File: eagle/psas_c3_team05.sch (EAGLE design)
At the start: 92 parts, among them IC1 CP2102, J1 3220-10-0100-00, J2 1.27MM_HDR_2X12X1, U1 MIC5319 3.3V, U2 MCP73871, U3 MKW01Z128, X1 32 MHz

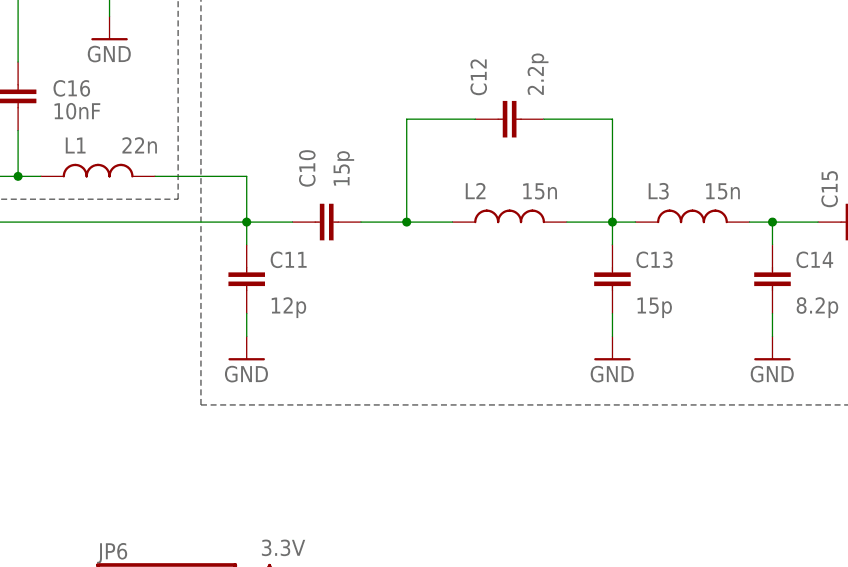
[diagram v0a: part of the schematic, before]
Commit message: Adding the last RF component values
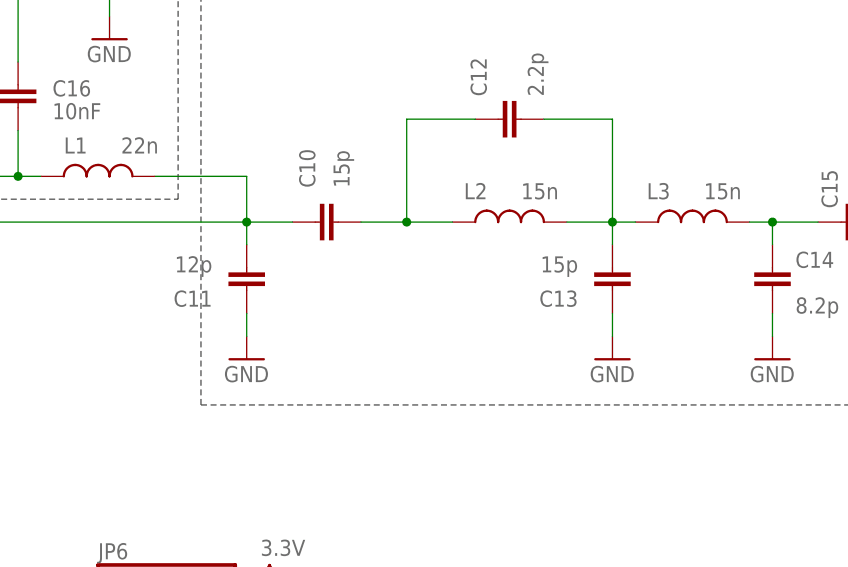
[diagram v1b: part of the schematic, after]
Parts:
- C10, C13: DIST (none) -> Digi-Key; DPN (none) -> 478-6024-1-ND; MFG (none) -> AVX; MFG-PN (none) -> 06031A150FAT2A
- C11: DIST (none) -> Mouser; DPN (none) -> 581-06035A120FAT2A; MFG (none) -> AVX; MFG-PN (none) -> 06035A120FAT2A
- C12: DIST (none) -> Mouser; DPN (none) -> 77-VJ0603A2R2BXJPBC; MFG (none) -> Vishay / Vitramon; MFG-PN (none) -> VJ0603A2R2BXJPW1BC
- C14: DIST (none) -> Mouser; DPN (none) -> 609-251R14S8R2BV4T; MFG (none) -> Johanson Technology; MFG-PN (none) -> 251R14S8R2BV4T
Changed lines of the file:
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@@
 <?xml version="1.0" encoding="utf-8"?>
 <!DOCTYPE eagle SYSTEM "eagle.dtd">
-<eagle version="7.3.0">
+<eagle version="7.4.0">
 <drawing>
 <settings>
@@
 <attribute name="MFG-PN" value="ZX62D-B-5P8"/>
 </part>
-<part name="C10" library="rcl_custom" deviceset="C-EU" device="0603-B-NOSILK" value="15p"/>
-<part name="C11" library="rcl_custom" deviceset="C-EU" device="0603-B-NOSILK" value="12p"/>
-<part name="C12" library="rcl_custom" deviceset="C-EU" device="0603-B-NOSILK" value="2.2p"/>
-<part name="C13" library="rcl_custom" deviceset="C-EU" device="0603-B-NOSILK" value="15p"/>
-<part name="C14" library="rcl_custom" deviceset="C-EU" device="0603-B-NOSILK" value="8.2p"/>
+<part name="C10" library="rcl_custom" deviceset="C-EU" device="0603-B-NOSILK" value="15p">
+<attribute name="DIST" value="Digi-Key"/>
+<attribute name="DPN" value="478-6024-1-ND"/>
+<attribute name="MFG" value="AVX"/>
+<attribute name="MFG-PN" value="06031A150FAT2A"/>
+</part>
+<part name="C12" library="rcl_custom" deviceset="C-EU" device="0603-B-NOSILK" value="2.2p">
+<attribute name="DIST" value="Mouser"/>
+<attribute name="DPN" value="77-VJ0603A2R2BXJPBC"/>
+<attribute name="MFG" value="Vishay / Vitramon"/>
+<attribute name="MFG-PN" value="VJ0603A2R2BXJPW1BC"/>
+</part>
+<part name="C14" library="rcl_custom" deviceset="C-EU" device="0603-B-NOSILK" value="8.2p">
+<attribute name="DIST" value="Mouser"/>
+<attribute name="DPN" value="609-251R14S8R2BV4T"/>
+<attribute name="MFG" value="Johanson Technology"/>
+<attribute name="MFG-PN" value="251R14S8R2BV4T"/>
+</part>
 <part name="GND17" library="Vibrogait_prototype" deviceset="GND" device=""/>
 <part name="GND18" library="Vibrogait_prototype" deviceset="GND" device=""/>
@@
 <part name="L1" library="rcl_custom" deviceset="L-US" device="0603-B-NOSILK" value="22n"/>
 <part name="L2" library="rcl_custom" deviceset="L-US" device="0603-B-NOSILK" value="15n"/>
-<part name="L3" library="rcl_custom" deviceset="L-US" device="0603-B-NOSILK" value="15n"/>
 <part name="GND21" library="Vibrogait_prototype" deviceset="GND" device=""/>
 <part name="IC1" library="silabs" deviceset="CP210*" device="" technology="2">
@@
 <part name="GND44" library="Vibrogait_prototype" deviceset="GND" device=""/>
 <part name="P+14" library="Vibrogait_prototype" deviceset="3.3V" device=""/>
+<part name="L3" library="rcl_custom" deviceset="L-US" device="0603-B-NOSILK" value="15n"/>
+<part name="C11" library="rcl_custom" deviceset="C-EU" device="0603-B-NOSILK" value="12p">
+<attribute name="DIST" value="Mouser"/>
+<attribute name="DPN" value="581-06035A120FAT2A"/>
+<attribute name="MFG" value="AVX"/>
+<attribute name="MFG-PN" value="06035A120FAT2A"/>
+</part>
+<part name="C13" library="rcl_custom" deviceset="C-EU" device="0603-B-NOSILK" value="15p">
+<attribute name="DIST" value="Digi-Key"/>
+<attribute name="DPN" value="478-6024-1-ND"/>
+<attribute name="MFG" value="AVX"/>
+<attribute name="MFG-PN" value="06031A150FAT2A"/>
+</part>
 </parts>
 <sheets>
@@
 <attribute name="NAME" x="403.86" y="222.25" size="1.778" layer="95" rot="R90"/>
 <attribute name="VALUE" x="407.67" y="222.25" size="1.778" layer="96" rot="R90"/>
-</instance>
-<instance part="C11" gate="CE" x="396.24" y="213.36" smashed="yes">
-<attribute name="NAME" x="398.78" y="213.36" size="1.778" layer="95"/>
-<attribute name="VALUE" x="398.78" y="208.28" size="1.778" layer="96"/>
+<attribute name="DIST" x="406.4" y="218.44" size="1.778" layer="96" rot="R270" display="off"/>
+<attribute name="MFG" x="406.4" y="218.44" size="1.778" layer="96" rot="R270" display="off"/>
+<attribute name="MFG-PN" x="406.4" y="218.44" size="1.778" layer="96" rot="R270" display="off"/>
+<attribute name="DPN" x="406.4" y="218.44" size="1.778" layer="96" rot="R270" display="off"/>
 </instance>
 <instance part="C12" gate="CE" x="426.72" y="229.87" smashed="yes" rot="R270">
 <attribute name="NAME" x="422.91" y="232.41" size="1.778" layer="95" rot="R90"/>
 <attribute name="VALUE" x="429.26" y="232.41" size="1.778" layer="96" rot="R90"/>
-</instance>
-<instance part="C13" gate="CE" x="436.88" y="213.36" smashed="yes">
-<attribute name="NAME" x="439.42" y="213.36" size="1.778" layer="95"/>
-<attribute name="VALUE" x="439.42" y="208.28" size="1.778" layer="96"/>
+<attribute name="DIST" x="426.72" y="229.87" size="1.778" layer="96" rot="R270" display="off"/>
+<attribute name="DPN" x="426.72" y="229.87" size="1.778" layer="96" rot="R270" display="off"/>
+<attribute name="MFG" x="426.72" y="229.87" size="1.778" layer="96" rot="R270" display="off"/>
+<attribute name="MFG-PN" x="426.72" y="229.87" size="1.778" layer="96" rot="R270" display="off"/>
 </instance>
 <instance part="C14" gate="CE" x="454.66" y="213.36" smashed="yes">
 <attribute name="NAME" x="457.2" y="213.36" size="1.778" layer="95"/>
 <attribute name="VALUE" x="457.2" y="208.28" size="1.778" layer="96"/>
+<attribute name="DIST" x="454.66" y="213.36" size="1.778" layer="96" display="off"/>
+<attribute name="DPN" x="454.66" y="213.36" size="1.778" layer="96" display="off"/>
+<attribute name="MFG" x="454.66" y="213.36" size="1.778" layer="96" display="off"/>
+<attribute name="MFG-PN" x="454.66" y="213.36" size="1.778" layer="96" display="off"/>
 </instance>
 <instance part="GND17" gate="1" x="396.24" y="203.2" smashed="yes">
@@
 <attribute name="NAME" x="420.37" y="220.98" size="1.778" layer="95"/>
 <attribute name="VALUE" x="426.72" y="220.98" size="1.778" layer="96" rot="MR180" align="top-left"/>
-</instance>
-<instance part="L3" gate="L" x="447.04" y="218.44" smashed="yes">
-<attribute name="NAME" x="440.69" y="220.98" size="1.778" layer="95"/>
-<attribute name="VALUE" x="447.04" y="220.98" size="1.778" layer="96" rot="MR180" align="top-left"/>
 </instance>
 <instance part="GND21" gate="1" x="246.38" y="121.92" smashed="yes">
@@
 <instance part="P+14" gate="G$1" x="492.76" y="302.26" smashed="yes">
 <attribute name="VALUE" x="491.744" y="305.816" size="1.778" layer="96"/>
+</instance>
+<instance part="L3" gate="L" x="447.04" y="218.44" smashed="yes">
+<attribute name="NAME" x="440.69" y="220.98" size="1.778" layer="95"/>
+<attribute name="VALUE" x="447.04" y="220.98" size="1.778" layer="96" rot="MR180" align="top-left"/>
+</instance>
+<instance part="C11" gate="CE" x="396.24" y="213.36" smashed="yes">
+<attribute name="NAME" x="392.43" y="210.82" size="1.778" layer="95" rot="R180"/>
+<attribute name="VALUE" x="392.43" y="214.63" size="1.778" layer="96" rot="R180"/>
+<attribute name="DIST" x="396.24" y="213.36" size="1.778" layer="96" display="off"/>
+<attribute name="MFG" x="396.24" y="213.36" size="1.778" layer="96" display="off"/>
+<attribute name="MFG-PN" x="396.24" y="213.36" size="1.778" layer="96" display="off"/>
+<attribute name="DPN" x="396.24" y="213.36" size="1.778" layer="96" display="off"/>
+</instance>
+<instance part="C13" gate="CE" x="436.88" y="213.36" smashed="yes">
+<attribute name="NAME" x="433.07" y="210.82" size="1.778" layer="95" rot="R180"/>
+<attribute name="VALUE" x="433.07" y="214.63" size="1.778" layer="96" rot="R180"/>
+<attribute name="DIST" x="436.88" y="213.36" size="1.778" layer="96" display="off"/>
+<attribute name="MFG" x="436.88" y="213.36" size="1.778" layer="96" display="off"/>
+<attribute name="MFG-PN" x="436.88" y="213.36" size="1.778" layer="96" display="off"/>
+<attribute name="DPN" x="436.88" y="213.36" size="1.778" layer="96" display="off"/>
 </instance>
 </instances>
@@
 </segment>
 <segment>
-<pinref part="C11" gate="CE" pin="2"/>
 <pinref part="GND17" gate="1" pin="GND"/>
 <wire x1="396.24" y1="208.28" x2="396.24" y2="205.74" width="0.1524" layer="91"/>
-</segment>
-<segment>
-<pinref part="C13" gate="CE" pin="2"/>
+<pinref part="C11" gate="CE" pin="2"/>
+</segment>
+<segment>
 <pinref part="GND19" gate="1" pin="GND"/>
 <wire x1="436.88" y1="208.28" x2="436.88" y2="205.74" width="0.1524" layer="91"/>
+<pinref part="C13" gate="CE" pin="2"/>
 </segment>
 <segment>
@@
 <wire x1="396.24" y1="223.52" x2="396.24" y2="218.44" width="0.1524" layer="91"/>
 <junction x="396.24" y="218.44"/>
+<wire x1="396.24" y1="215.9" x2="396.24" y2="218.44" width="0.1524" layer="91"/>
 <pinref part="C11" gate="CE" pin="1"/>
-<wire x1="396.24" y1="215.9" x2="396.24" y2="218.44" width="0.1524" layer="91"/>
 </segment>
 </net>
 <net name="N$17" class="0">
 <segment>
-<pinref part="C13" gate="CE" pin="1"/>
 <wire x1="436.88" y1="215.9" x2="436.88" y2="218.44" width="0.1524" layer="91"/>
 <junction x="436.88" y="218.44"/>
@@
 <pinref part="L2" gate="L" pin="2"/>
 <wire x1="431.8" y1="218.44" x2="436.88" y2="218.44" width="0.1524" layer="91"/>
+<wire x1="436.88" y1="218.44" x2="439.42" y2="218.44" width="0.1524" layer="91"/>
 <pinref part="L3" gate="L" pin="1"/>
-<wire x1="436.88" y1="218.44" x2="439.42" y2="218.44" width="0.1524" layer="91"/>
+<pinref part="C13" gate="CE" pin="1"/>
 </segment>
 </net>
@@
 <wire x1="454.66" y1="218.44" x2="459.74" y2="218.44" width="0.1524" layer="91"/>
 <wire x1="454.66" y1="218.44" x2="454.66" y2="215.9" width="0.1524" layer="91"/>
-<pinref part="L3" gate="L" pin="2"/>
 <wire x1="452.12" y1="218.44" x2="454.66" y2="218.44" width="0.1524" layer="91"/>
 <junction x="454.66" y="218.44"/>
+<pinref part="L3" gate="L" pin="2"/>
 </segment>
 </net>

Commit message: Added final part attrib RF
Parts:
- C15: DIST (none) -> Digi-Key; DPN 490-1532-1-ND -> 478-5778-1-ND; MFG (none) -> AVX; MFG-PN (none) -> 06035C104JAT2A
- C16: DIST (none) -> Digi-Key; DPN (none) -> 478-6208-1-ND; MFG (none) -> AVX; MFG-PN (none) -> 0603YC103JAT2A
- L1: DIST (none) -> Digi-Key; DPN (none) -> 490-6874-1-ND; MFG (none) -> Murata; MFG-PN (none) -> LQW18AN22NG00D
- L2, L3: DIST (none) -> Digi-Key; DPN (none) -> 490-6866-1-ND; MFG (none) -> Murata; MFG-PN (none) -> LQW18AN15NG00D
- U$2: DIST (none) -> Digi-Key; DPN (none) -> J716-ND; MFG (none) -> Cinch Connectivity Solutions; MFG-PN (none) -> 142-0701-806
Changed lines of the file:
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@@
 <part name="GND19" library="Vibrogait_prototype" deviceset="GND" device=""/>
 <part name="C15" library="rcl_custom" deviceset="C-EU" device="0603-B-NOSILK" value="100nF">
-<attribute name="DPN" value="490-1532-1-ND"/>
-</part>
-<part name="C16" library="rcl_custom" deviceset="C-EU" device="0603-B-NOSILK" value="10nF"/>
+<attribute name="DIST" value="Digi-Key"/>
+<attribute name="DPN" value="478-5778-1-ND"/>
+<attribute name="MFG" value="AVX"/>
+<attribute name="MFG-PN" value="06035C104JAT2A"/>
+</part>
+<part name="C16" library="rcl_custom" deviceset="C-EU" device="0603-B-NOSILK" value="10nF">
+<attribute name="DIST" value="Digi-Key"/>
+<attribute name="DPN" value="478-6208-1-ND"/>
+<attribute name="MFG" value="AVX"/>
+<attribute name="MFG-PN" value="0603YC103JAT2A"/>
+</part>
 <part name="GND20" library="Vibrogait_prototype" deviceset="GND" device=""/>
-<part name="L1" library="rcl_custom" deviceset="L-US" device="0603-B-NOSILK" value="22n"/>
-<part name="L2" library="rcl_custom" deviceset="L-US" device="0603-B-NOSILK" value="15n"/>
+<part name="L1" library="rcl_custom" deviceset="L-US" device="0603-B-NOSILK" value="22n">
+<attribute name="DIST" value="Digi-Key"/>
+<attribute name="DPN" value="490-6874-1-ND"/>
+<attribute name="MFG" value="Murata"/>
+<attribute name="MFG-PN" value="LQW18AN22NG00D"/>
+</part>
+<part name="L2" library="rcl_custom" deviceset="L-US" device="0603-B-NOSILK" value="15n">
+<attribute name="DIST" value="Digi-Key"/>
+<attribute name="DPN" value="490-6866-1-ND"/>
+<attribute name="MFG" value="Murata"/>
+<attribute name="MFG-PN" value="LQW18AN15NG00D"/>
+</part>
 <part name="GND21" library="Vibrogait_prototype" deviceset="GND" device=""/>
 <part name="IC1" library="silabs" deviceset="CP210*" device="" technology="2">
@@
 <attribute name="MPN" value="GRM188R71C104KA01D"/>
 </part>
-<part name="U$2" library="SMAJ16-ND" deviceset="SMAJ716-ND" device=""/>
+<part name="U$2" library="SMAJ16-ND" deviceset="SMAJ716-ND" device="">
+<attribute name="DIST" value="Digi-Key"/>
+<attribute name="DPN" value="J716-ND"/>
+<attribute name="MFG" value="Cinch Connectivity Solutions"/>
+<attribute name="MFG-PN" value="142-0701-806"/>
+</part>
 <part name="P+6" library="Vibrogait_prototype" deviceset="3.3V" device=""/>
 <part name="TP6" library="microbuilder" deviceset="TESTPOINT" device="ROUND0.5MM"/>
@@
 <part name="GND44" library="Vibrogait_prototype" deviceset="GND" device=""/>
 <part name="P+14" library="Vibrogait_prototype" deviceset="3.3V" device=""/>
-<part name="L3" library="rcl_custom" deviceset="L-US" device="0603-B-NOSILK" value="15n"/>
 <part name="C11" library="rcl_custom" deviceset="C-EU" device="0603-B-NOSILK" value="12p">
 <attribute name="DIST" value="Mouser"/>
@@
 <attribute name="MFG" value="AVX"/>
 <attribute name="MFG-PN" value="06031A150FAT2A"/>
+</part>
+<part name="L3" library="rcl_custom" deviceset="L-US" device="0603-B-NOSILK" value="15n">
+<attribute name="DIST" value="Digi-Key"/>
+<attribute name="DPN" value="490-6866-1-ND"/>
+<attribute name="MFG" value="Murata"/>
+<attribute name="MFG-PN" value="LQW18AN15NG00D"/>
 </part>
 </parts>
@@
 <attribute name="VALUE" x="466.979" y="219.964" size="1.778" layer="96" rot="R90"/>
 <attribute name="DPN" x="462.28" y="218.44" size="1.778" layer="96" rot="R90" display="off"/>
+<attribute name="DIST" x="462.28" y="218.44" size="1.778" layer="96" rot="R90" display="off"/>
+<attribute name="MFG" x="462.28" y="218.44" size="1.778" layer="96" rot="R90" display="off"/>
+<attribute name="MFG-PN" x="462.28" y="218.44" size="1.778" layer="96" rot="R90" display="off"/>
 </instance>
 <instance part="C16" gate="CE" x="370.84" y="233.68" smashed="yes">
 <attribute name="NAME" x="374.65" y="232.41" size="1.778" layer="95"/>
 <attribute name="VALUE" x="374.65" y="229.87" size="1.778" layer="96"/>
+<attribute name="DIST" x="370.84" y="233.68" size="1.778" layer="96" display="off"/>
+<attribute name="DPN" x="370.84" y="233.68" size="1.778" layer="96" display="off"/>
+<attribute name="MFG" x="370.84" y="233.68" size="1.778" layer="96" display="off"/>
+<attribute name="MFG-PN" x="370.84" y="233.68" size="1.778" layer="96" display="off"/>
 </instance>
 <instance part="GND20" gate="1" x="381" y="238.76" smashed="yes">
@@
 <attribute name="NAME" x="375.92" y="226.06" size="1.778" layer="95"/>
 <attribute name="VALUE" x="382.27" y="226.06" size="1.778" layer="96" rot="MR180" align="top-left"/>
+<attribute name="DIST" x="381" y="223.52" size="1.778" layer="96" display="off"/>
+<attribute name="DPN" x="381" y="223.52" size="1.778" layer="96" display="off"/>
+<attribute name="MFG" x="381" y="223.52" size="1.778" layer="96" display="off"/>
+<attribute name="MFG-PN" x="381" y="223.52" size="1.778" layer="96" display="off"/>
 </instance>
 <instance part="L2" gate="L" x="426.72" y="218.44" smashed="yes">
 <attribute name="NAME" x="420.37" y="220.98" size="1.778" layer="95"/>
 <attribute name="VALUE" x="426.72" y="220.98" size="1.778" layer="96" rot="MR180" align="top-left"/>
+<attribute name="DIST" x="426.72" y="218.44" size="1.778" layer="96" display="off"/>
+<attribute name="DPN" x="426.72" y="218.44" size="1.778" layer="96" display="off"/>
+<attribute name="MFG" x="426.72" y="218.44" size="1.778" layer="96" display="off"/>
+<attribute name="MFG-PN" x="426.72" y="218.44" size="1.778" layer="96" display="off"/>
 </instance>
 <instance part="GND21" gate="1" x="246.38" y="121.92" smashed="yes">
@@
 <attribute name="VALUE" x="192.024" y="231.521" size="1.778" layer="96"/>
 </instance>
-<instance part="U$2" gate="G$1" x="487.68" y="218.44" smashed="yes" rot="MR0"/>
+<instance part="U$2" gate="G$1" x="487.68" y="218.44" smashed="yes" rot="MR0">
+<attribute name="DIST" x="487.68" y="218.44" size="1.778" layer="96" rot="MR0" display="off"/>
+<attribute name="DPN" x="487.68" y="218.44" size="1.778" layer="96" rot="MR0" display="off"/>
+<attribute name="MFG" x="487.68" y="218.44" size="1.778" layer="96" rot="MR0" display="off"/>
+<attribute name="MFG-PN" x="487.68" y="218.44" size="1.778" layer="96" rot="MR0" display="off"/>
+</instance>
 <instance part="P+6" gate="G$1" x="317.5" y="226.06" smashed="yes">
 <attribute name="VALUE" x="315.595" y="228.854" size="1.778" layer="96"/>
@@
 <attribute name="VALUE" x="491.744" y="305.816" size="1.778" layer="96"/>
 </instance>
-<instance part="L3" gate="L" x="447.04" y="218.44" smashed="yes">
-<attribute name="NAME" x="440.69" y="220.98" size="1.778" layer="95"/>
-<attribute name="VALUE" x="447.04" y="220.98" size="1.778" layer="96" rot="MR180" align="top-left"/>
-</instance>
 <instance part="C11" gate="CE" x="396.24" y="213.36" smashed="yes">
 <attribute name="NAME" x="392.43" y="210.82" size="1.778" layer="95" rot="R180"/>
@@
 <attribute name="MFG-PN" x="436.88" y="213.36" size="1.778" layer="96" display="off"/>
 <attribute name="DPN" x="436.88" y="213.36" size="1.778" layer="96" display="off"/>
+</instance>
+<instance part="L3" gate="L" x="447.04" y="218.44" smashed="yes">
+<attribute name="NAME" x="440.69" y="220.98" size="1.778" layer="95"/>
+<attribute name="VALUE" x="447.04" y="220.98" size="1.778" layer="96" rot="MR180" align="top-left"/>
+<attribute name="DIST" x="447.04" y="218.44" size="1.778" layer="96" display="off"/>
+<attribute name="DPN" x="447.04" y="218.44" size="1.778" layer="96" display="off"/>
+<attribute name="MFG" x="447.04" y="218.44" size="1.778" layer="96" display="off"/>
+<attribute name="MFG-PN" x="447.04" y="218.44" size="1.778" layer="96" display="off"/>
 </instance>
 </instances>
@@
 <wire x1="431.8" y1="218.44" x2="436.88" y2="218.44" width="0.1524" layer="91"/>
 <wire x1="436.88" y1="218.44" x2="439.42" y2="218.44" width="0.1524" layer="91"/>
+<pinref part="C13" gate="CE" pin="1"/>
 <pinref part="L3" gate="L" pin="1"/>
-<pinref part="C13" gate="CE" pin="1"/>
 </segment>
 </net>

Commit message: added attributes to crystal
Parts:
- X1: DIST (none) -> Digi-Key; DPN SER3672CT-ND -> 1253-1161-1-ND; DPN2 (none) -> CTX1364CT-ND; MFG (none) -> AVX Corp/Kyocera Corp; MFG-PN (none) -> CX3225GA32000D0PTVCC; MFG2 (none) -> CTS-Frequency Controls; MFG2-PN (none) -> 402F3201XIAR
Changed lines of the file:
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@@
 <?xml version="1.0" encoding="utf-8"?>
 <!DOCTYPE eagle SYSTEM "eagle.dtd">
-<eagle version="7.4.0">
+<eagle version="7.3.0">
 <drawing>
 <settings>
@@
 <part name="GND27" library="Vibrogait_prototype" deviceset="GND" device=""/>
 <part name="X1" library="crystal" deviceset="FC-12M" device="" value="32 MHz">
-<attribute name="DPN" value="SER3672CT-ND"/>
+<attribute name="DIST" value="Digi-Key"/>
+<attribute name="DPN" value="1253-1161-1-ND"/>
+<attribute name="DPN2" value="CTX1364CT-ND"/>
+<attribute name="MFG" value="AVX Corp/Kyocera Corp"/>
+<attribute name="MFG-PN" value="CX3225GA32000D0PTVCC"/>
+<attribute name="MFG2" value="CTS-Frequency Controls"/>
+<attribute name="MFG2-PN" value="402F3201XIAR"/>
 </part>
 <part name="R6" library="rcl_custom" deviceset="R-US_" device="0603-B-NOSILK" value="0"/>
@@
 <attribute name="VALUE" x="324.2056" y="195.0466" size="1.778" layer="96"/>
 <attribute name="DPN" x="328.93" y="193.04" size="1.778" layer="96" rot="R180" display="off"/>
+<attribute name="DIST" x="328.93" y="193.04" size="1.778" layer="96" rot="R180" display="off"/>
+<attribute name="MFG" x="328.93" y="193.04" size="1.778" layer="96" rot="R180" display="off"/>
+<attribute name="MFG-PN" x="328.93" y="193.04" size="1.778" layer="96" rot="R180" display="off"/>
+<attribute name="DPN2" x="328.93" y="193.04" size="1.778" layer="96" rot="R180" display="off"/>
+<attribute name="MFG2" x="328.93" y="193.04" size="1.778" layer="96" rot="R180" display="off"/>
+<attribute name="MFG2-PN" x="328.93" y="193.04" size="1.778" layer="96" rot="R180" display="off"/>
 </instance>
 <instance part="R6" gate="R" x="312.42" y="193.04" smashed="yes" rot="R180">
